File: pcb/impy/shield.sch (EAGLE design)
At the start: 129 parts, among them J1 USB-2410-06, J2 SI-60062-F, J3 5V, U1 AD5933YRS, U10 LTC3406AB, U11 23LCV1024-I/SN, U12 MIC2009A-1YM6, U13 ADG725BSU, U14 ADG725BSU, U2 ADG704BRM, U3 AD8656ARZ, U4 M24C08WMN, U5 ADG706BRU, U6 DP83848I, U7 MIC2009A-1YM6, U8 AT25DF081A-SS, U9 SST25VF080B-80-4I-S2

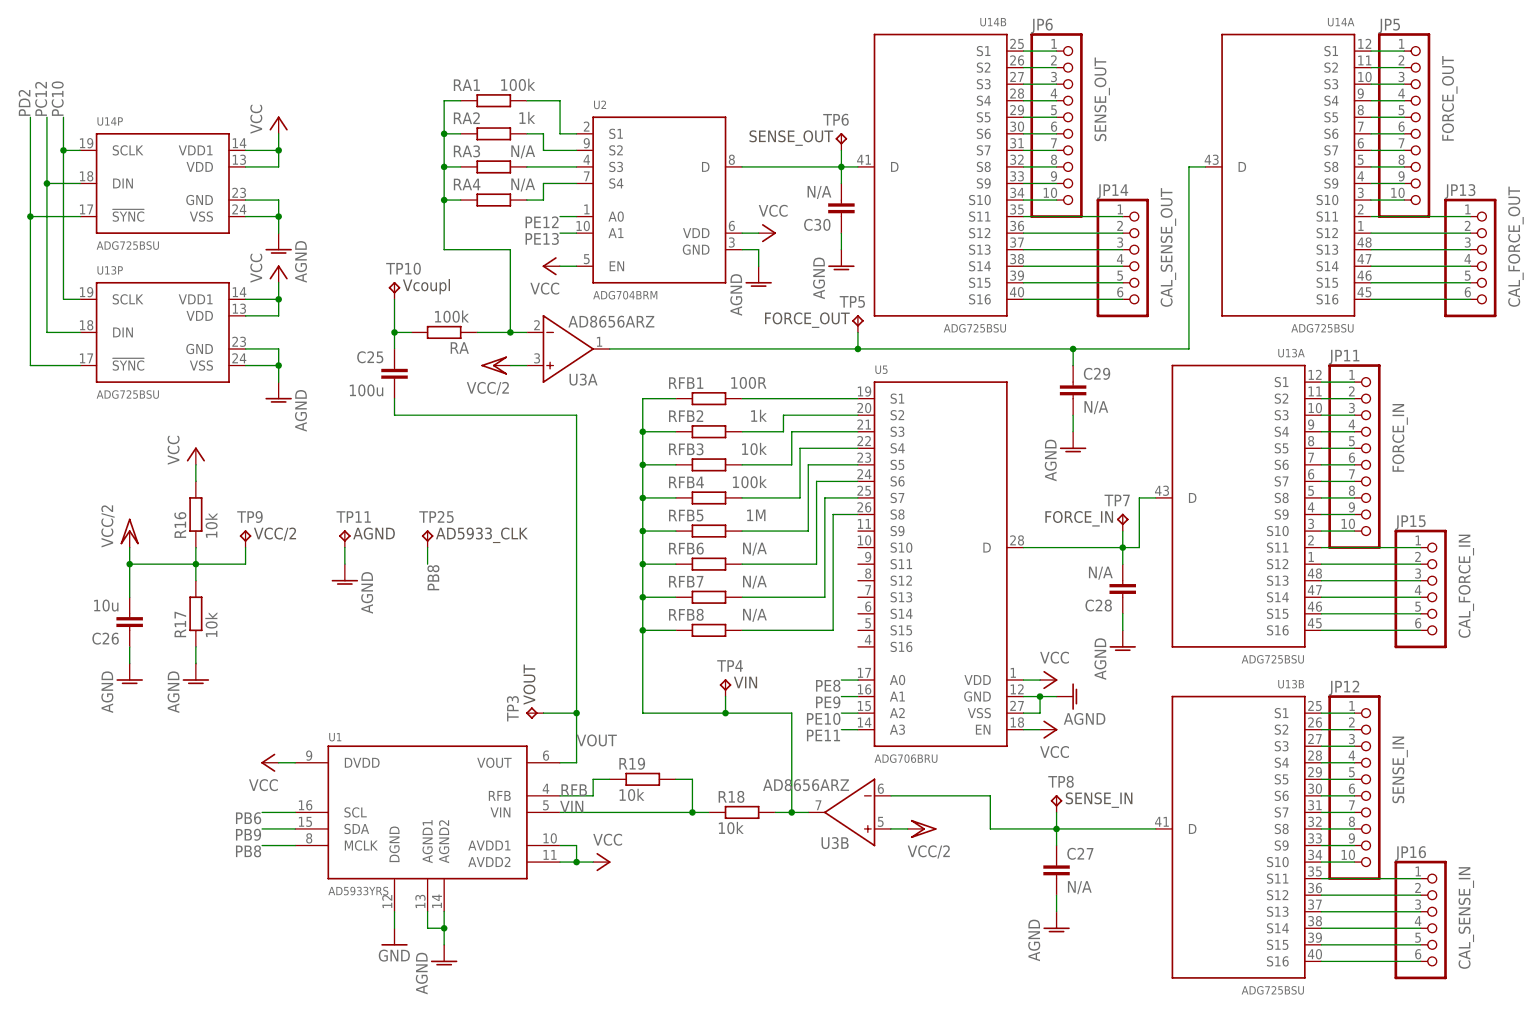
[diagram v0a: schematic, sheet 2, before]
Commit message: * pcb/impy: (shield.sch) Add pullup to 16:1 multiplexer enable pin.   (shield.brd) Layout some more analog stuff.
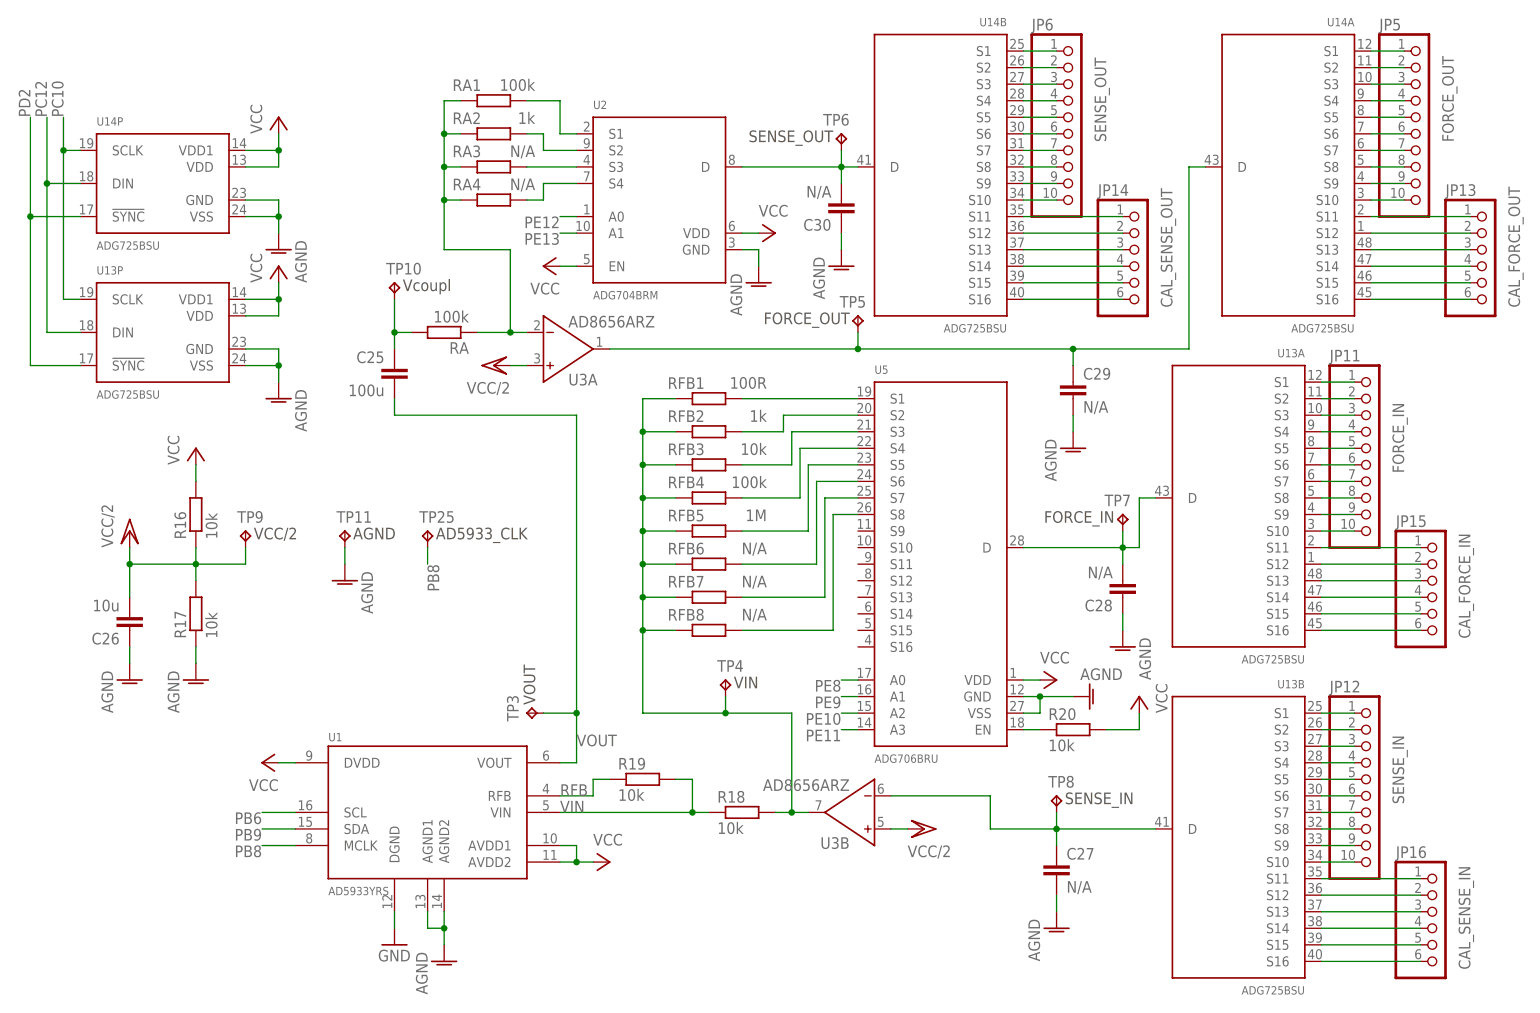
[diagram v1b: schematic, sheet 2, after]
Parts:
- added R20: 10k, rcl:R-EU_R0603
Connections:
- new net N$107: R20.1, U5.EN
- net N$103: now also RA1.2; no longer RA1.1
- net N$3: now also RA1.1; no longer RA1.2
- net VCC: now also R20.2; no longer U5.EN
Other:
- moved on the sheet: RA1
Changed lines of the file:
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@@
 <attribute name="TP_SIGNAL_NAME" value="AD5933_CLK"/>
 </part>
+<part name="R20" library="rcl" deviceset="R-EU_" device="R0603" value="10k"/>
 </parts>
 <sheets>
@@
 <instance part="C25" gate="G$1" x="43.18" y="114.3" rot="MR0"/>
 <instance part="RA" gate="G$1" x="50.8" y="119.38" rot="R180"/>
-<instance part="RA1" gate="G$1" x="58.42" y="154.94" smashed="yes" rot="R180">
+<instance part="RA1" gate="G$1" x="58.42" y="154.94" smashed="yes">
 <attribute name="NAME" x="52.07" y="156.4386" size="1.778" layer="95"/>
 <attribute name="VALUE" x="64.77" y="158.242" size="1.778" layer="96" rot="R180"/>
@@
 <instance part="U5" gate="G$1" x="127" y="83.82"/>
 <instance part="P+32" gate="VCC" x="144.78" y="66.04" rot="R270"/>
-<instance part="P+33" gate="VCC" x="144.78" y="58.42" rot="MR90"/>
-<instance part="AGND7" gate="VR1" x="147.32" y="63.5" rot="R90"/>
+<instance part="P+33" gate="VCC" x="157.48" y="63.5" rot="MR0"/>
+<instance part="AGND7" gate="VR1" x="149.86" y="63.5" rot="MR270"/>
 <instance part="RFB1" gate="G$1" x="91.44" y="109.22" smashed="yes" rot="R180">
 <attribute name="NAME" x="85.09" y="110.7186" size="1.778" layer="95"/>
@@
 <instance part="C30" gate="G$1" x="111.76" y="137.16" rot="R180"/>
 <instance part="AGND10" gate="VR1" x="144.78" y="27.94"/>
-<instance part="AGND11" gate="VR1" x="154.94" y="71.12"/>
+<instance part="AGND11" gate="VR1" x="154.94" y="71.12" rot="MR0"/>
 <instance part="AGND12" gate="VR1" x="147.32" y="101.6"/>
 <instance part="AGND13" gate="VR1" x="111.76" y="129.54"/>
@@
 <instance part="AGND14" gate="VR1" x="35.56" y="81.28" rot="MR0"/>
 <instance part="TP25" gate="G$1" x="48.26" y="88.9"/>
+<instance part="R20" gate="G$1" x="147.32" y="58.42"/>
 </instances>
 <busses>
@@
 </segment>
 <segment>
-<pinref part="P+33" gate="VCC" pin="VCC"/>
-<pinref part="U5" gate="G$1" pin="EN"/>
-<wire x1="142.24" y1="58.42" x2="139.7" y2="58.42" width="0.1524" layer="91"/>
-</segment>
-<segment>
 <pinref part="P+34" gate="VCC" pin="VCC"/>
 <pinref part="U14" gate="P" pin="VDD"/>
@@
 <junction x="25.4" y="124.46"/>
 </segment>
+<segment>
+<pinref part="R20" gate="G$1" pin="2"/>
+<pinref part="P+33" gate="VCC" pin="VCC"/>
+<wire x1="152.4" y1="58.42" x2="157.48" y2="58.42" width="0.1524" layer="91"/>
+<wire x1="157.48" y1="58.42" x2="157.48" y2="60.96" width="0.1524" layer="91"/>
+</segment>
 </net>
 <net name="GND" class="1">
@@
 <wire x1="139.7" y1="63.5" x2="142.24" y2="63.5" width="0.1524" layer="91"/>
 <pinref part="U5" gate="G$1" pin="VSS"/>
-<wire x1="142.24" y1="63.5" x2="144.78" y2="63.5" width="0.1524" layer="91"/>
+<wire x1="142.24" y1="63.5" x2="147.32" y2="63.5" width="0.1524" layer="91"/>
 <wire x1="139.7" y1="60.96" x2="142.24" y2="60.96" width="0.1524" layer="91"/>
 <wire x1="142.24" y1="60.96" x2="142.24" y2="63.5" width="0.1524" layer="91"/>
@@
 <net name="N$3" class="2">
 <segment>
-<pinref part="RA1" gate="G$1" pin="2"/>
+<pinref part="RA1" gate="G$1" pin="1"/>
 <wire x1="50.8" y1="139.7" x2="50.8" y2="144.78" width="0.1524" layer="91"/>
 <wire x1="50.8" y1="144.78" x2="50.8" y2="149.86" width="0.1524" layer="91"/>
@@
 <wire x1="71.12" y1="149.86" x2="68.58" y2="149.86" width="0.1524" layer="91"/>
 <wire x1="68.58" y1="149.86" x2="68.58" y2="154.94" width="0.1524" layer="91"/>
-<pinref part="RA1" gate="G$1" pin="1"/>
+<pinref part="RA1" gate="G$1" pin="2"/>
 <wire x1="68.58" y1="154.94" x2="63.5" y2="154.94" width="0.1524" layer="91"/>
 </segment>
@@
 </segment>
 </net>
+<net name="N$107" class="0">
+<segment>
+<pinref part="R20" gate="G$1" pin="1"/>
+<pinref part="U5" gate="G$1" pin="EN"/>
+<wire x1="142.24" y1="58.42" x2="139.7" y2="58.42" width="0.1524" layer="91"/>
+</segment>
+</net>

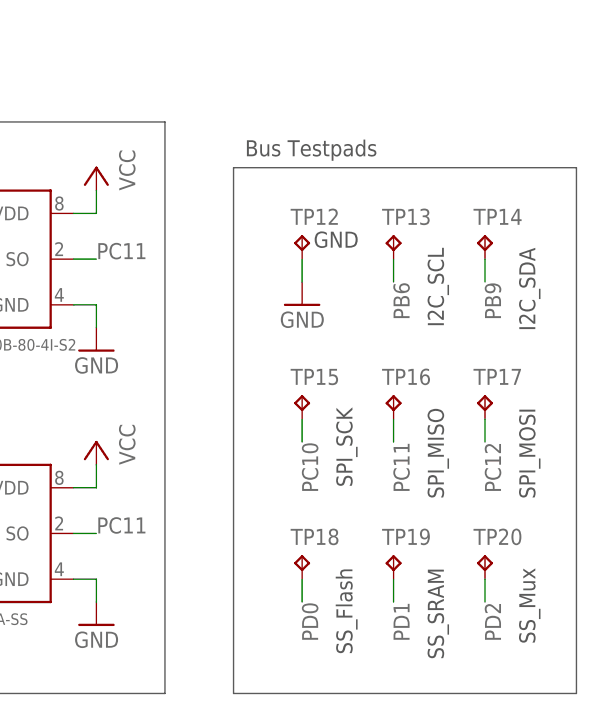
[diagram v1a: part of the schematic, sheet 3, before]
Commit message: * pcb/impy: (shield.sch) Remove unnecessary test pads, all of these signals can be accessed from the discovery board connector anyway.
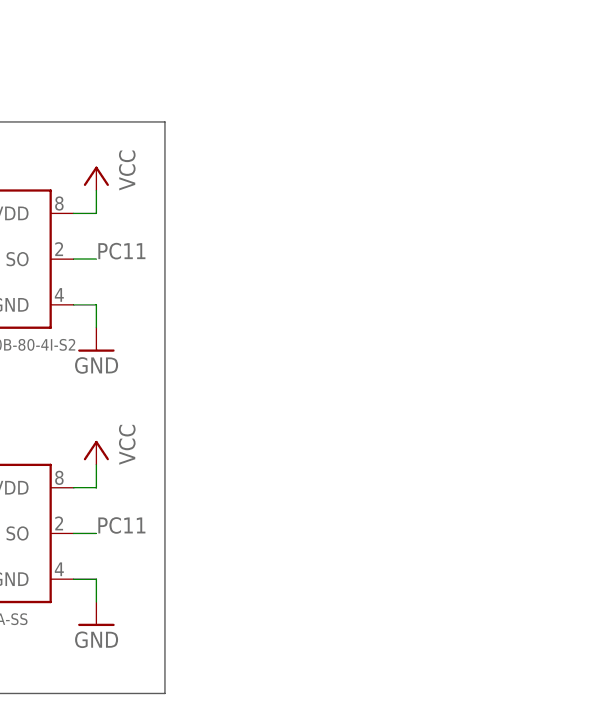
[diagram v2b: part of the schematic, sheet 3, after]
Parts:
- removed TP15, TP16, TP17, TP18, TP19, TP20, TP21, TP22, TP23, TP24, TP25: TPTP20R, testpad:TPTP20R
- TP12: TP_SIGNAL_NAME GND -> AD5933_CLK
- TP13: TP_SIGNAL_NAME I2C_SCL -> USBH_VBUS
- TP14: TP_SIGNAL_NAME I2C_SDA -> MAC_CLK
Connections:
- net GND: no longer TP12.TP
- net N$106: now also TP14.TP; no longer TP22.TP
- net N$26: now also TP13.TP; no longer TP21.TP
- net PA2: no longer TP24.TP
- net PB6: no longer TP13.TP
- net PB8: now also TP12.TP; no longer TP25.TP
- net PB9: no longer TP14.TP
- net PC1: no longer TP23.TP
- net PC10: no longer TP15.TP
- net PC11: no longer TP16.TP
- net PC12: no longer TP17.TP
- net PD0: no longer TP18.TP
- net PD1: no longer TP19.TP
- net PD2: no longer TP20.TP
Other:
- note removed: "Bus Testpads"

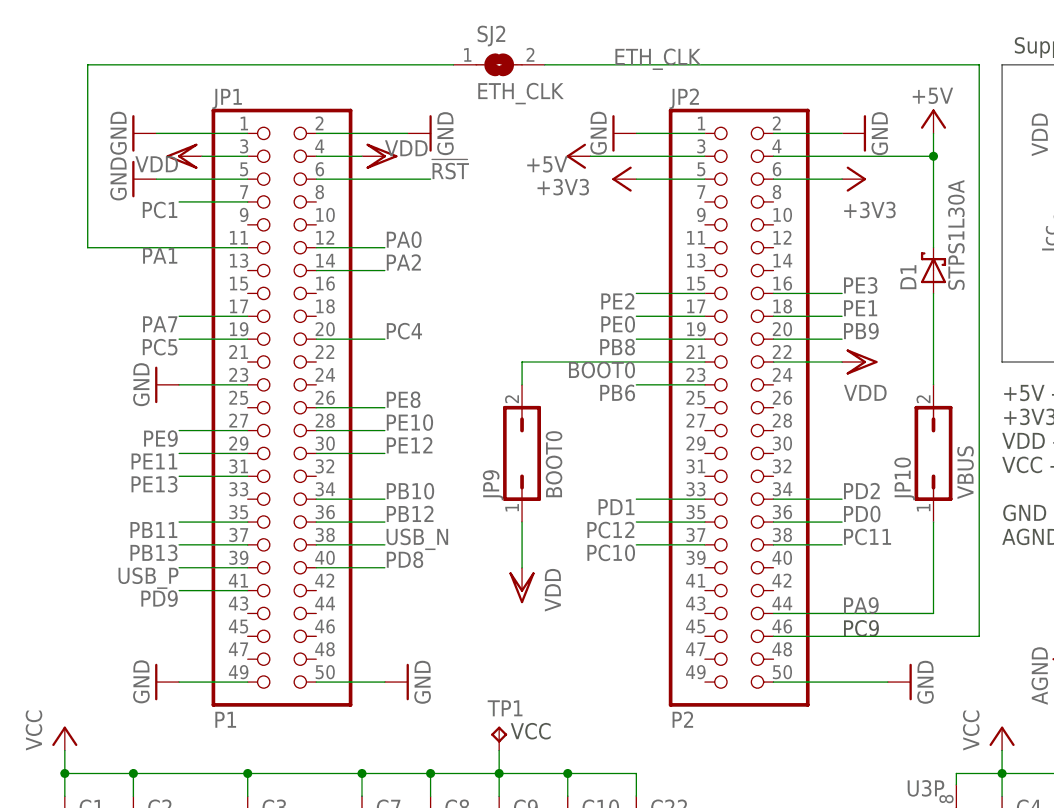
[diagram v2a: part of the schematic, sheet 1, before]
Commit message: * pcb/impy: (shield.sch) Change ETH_CLK net to be after the solder jumper (PA1 instead of PC9).
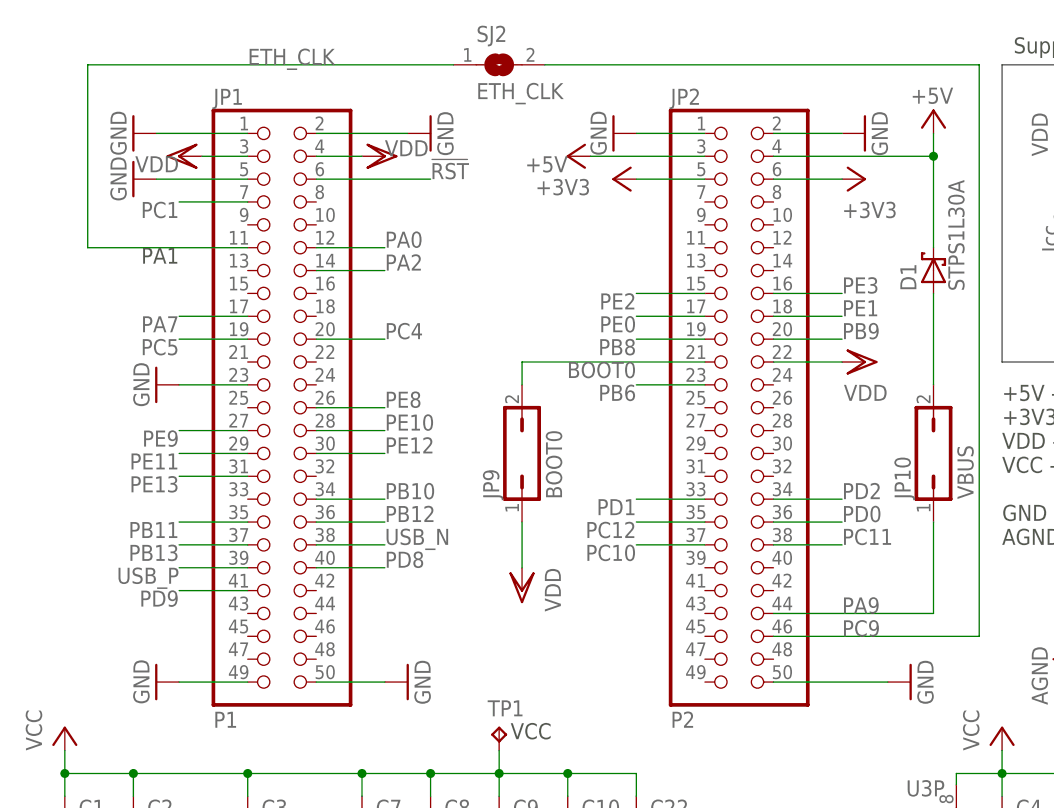
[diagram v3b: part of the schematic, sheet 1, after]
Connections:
- removed net PA1: JP1.11, SJ2.1
- new net PC9: JP2.46, SJ2.2
- net ETH_CLK: now also JP1.11, SJ2.1; no longer JP2.46, SJ2.2
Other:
- note added: "PA1"
- note removed: "PC9"
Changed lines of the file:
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@@
 <wire x1="104.14" y1="55.88" x2="104.14" y2="88.9" width="0.1524" layer="97"/>
 <text x="105.41" y="90.17" size="1.778" layer="97">Supply Current Measurement + Power Switch</text>
-<text x="86.36" y="25.4" size="1.778" layer="97">PC9</text>
+<text x="12.7" y="68.58" size="1.778" layer="97" rot="R180">PA1</text>
 <wire x1="208.28" y1="83.82" x2="172.72" y2="83.82" width="0.1524" layer="97"/>
 <wire x1="172.72" y1="83.82" x2="172.72" y2="45.72" width="0.1524" layer="97"/>
@@
 <wire x1="78.74" y1="35.56" x2="86.36" y2="35.56" width="0.1524" layer="91"/>
 <label x="86.36" y="35.56" size="1.778" layer="95"/>
-</segment>
-</net>
-<net name="ETH_CLK" class="0">
-<segment>
-<pinref part="JP2" gate="A" pin="46"/>
-<label x="60.96" y="88.9" size="1.778" layer="95"/>
-<wire x1="78.74" y1="25.4" x2="101.6" y2="25.4" width="0.1524" layer="91"/>
-<wire x1="101.6" y1="25.4" x2="101.6" y2="88.9" width="0.1524" layer="91"/>
-<wire x1="101.6" y1="88.9" x2="53.34" y2="88.9" width="0.1524" layer="91"/>
-<pinref part="SJ2" gate="1" pin="2"/>
 </segment>
 </net>
@@
 </segment>
 </net>
-<net name="PA1" class="0">
+<net name="ETH_CLK" class="0">
 <segment>
 <pinref part="JP1" gate="A" pin="11"/>
@@
 <wire x1="2.54" y1="68.58" x2="20.32" y2="68.58" width="0.1524" layer="91"/>
 <pinref part="SJ2" gate="1" pin="1"/>
-<label x="12.7" y="68.58" size="1.778" layer="95" rot="R180"/>
+<label x="20.32" y="88.9" size="1.778" layer="95"/>
 </segment>
 </net>
@@
 </segment>
 </net>
+<net name="PC9" class="0">
+<segment>
+<pinref part="JP2" gate="A" pin="46"/>
+<label x="86.36" y="25.4" size="1.778" layer="95"/>
+<wire x1="78.74" y1="25.4" x2="101.6" y2="25.4" width="0.1524" layer="91"/>
+<wire x1="101.6" y1="25.4" x2="101.6" y2="88.9" width="0.1524" layer="91"/>
+<wire x1="101.6" y1="88.9" x2="53.34" y2="88.9" width="0.1524" layer="91"/>
+<pinref part="SJ2" gate="1" pin="2"/>
+</segment>
+</net>
